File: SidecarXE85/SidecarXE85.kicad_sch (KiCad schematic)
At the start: 11 parts, among them J1 DE9_Plug, J2 DE9_Plug, J3 DE9_Receptacle, J4 Conn_02x08_Odd_Even, J5 DE9_Receptacle, SW1 SW_SPDT, U1 MM74C923, U2 74AHC04

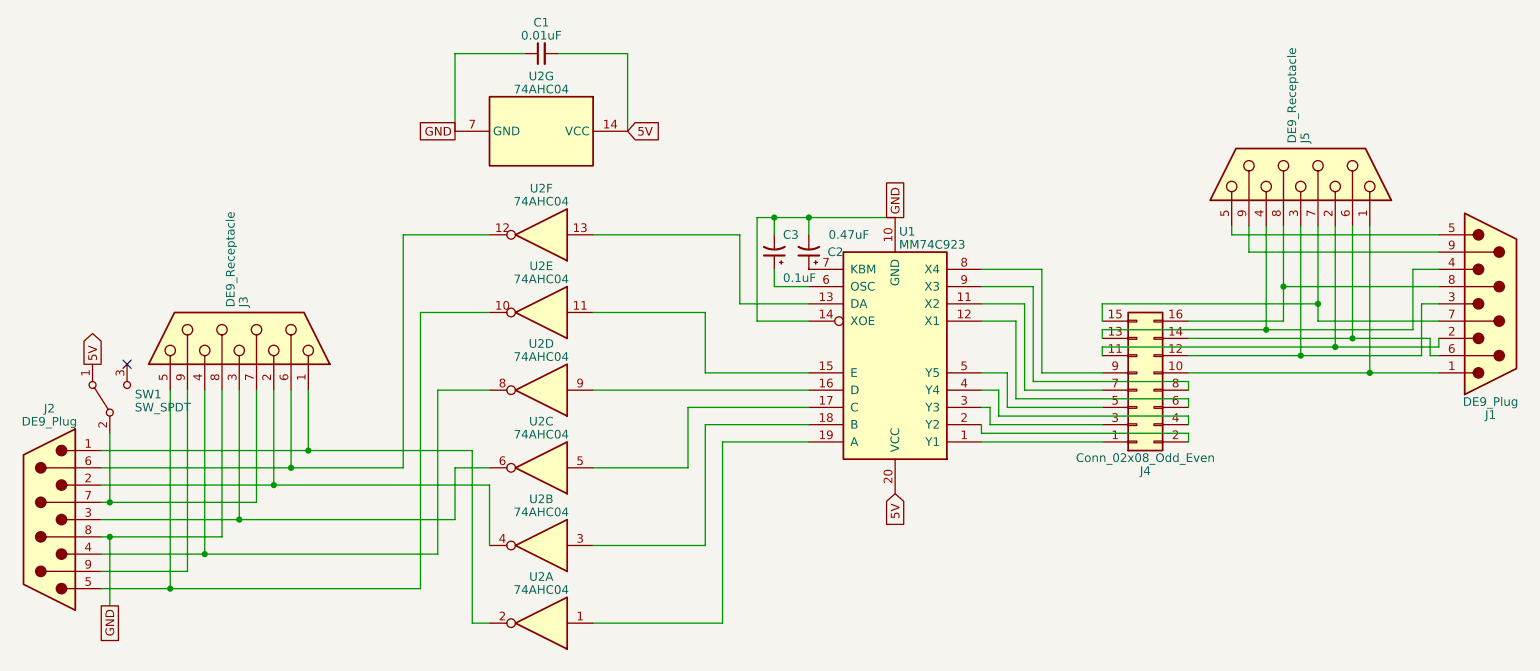
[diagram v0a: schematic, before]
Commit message: Sidecar control board revision 2
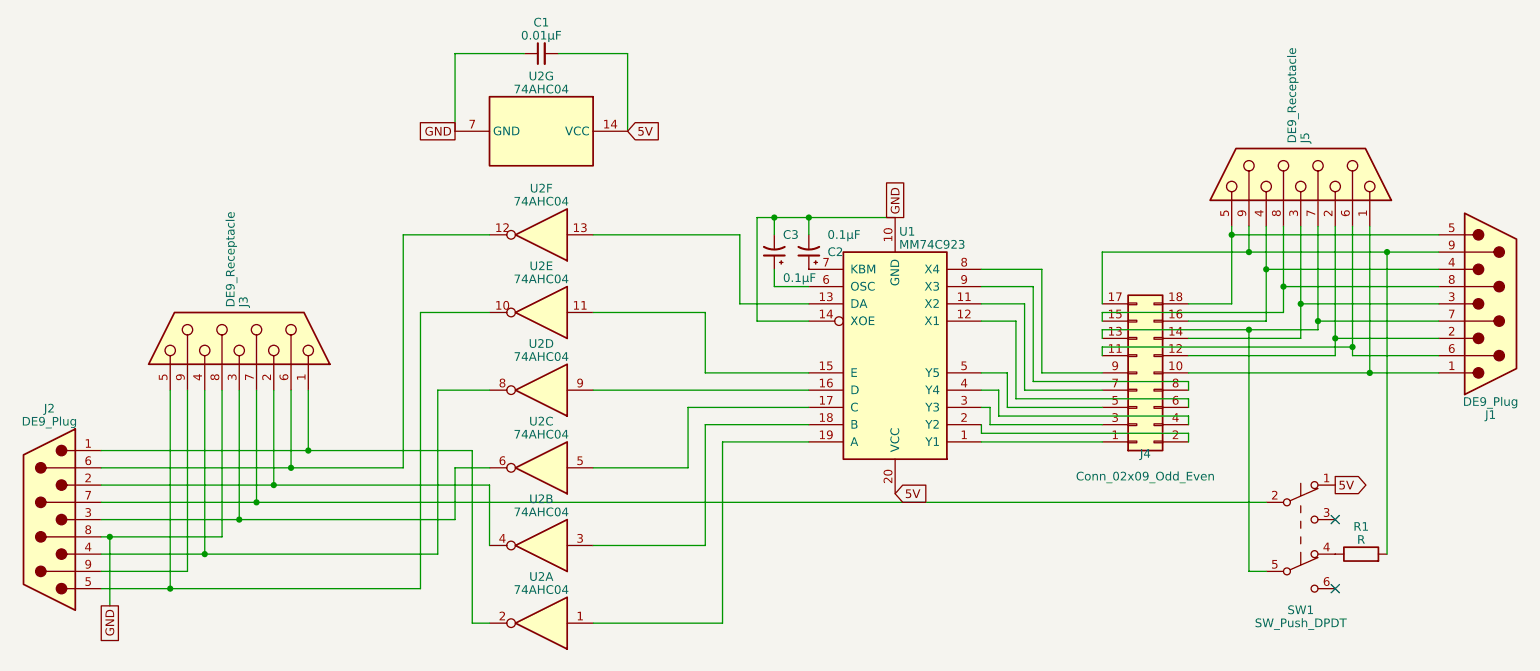
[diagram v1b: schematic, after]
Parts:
- removed SW1: SW_SPDT, Connector_PinHeader_2.54mm:PinHeader_1x03_P2.54mm_Vertical, symbol Switch:SW_SPDT
- added R1: R, Resistor_THT:R_Axial_DIN0207_L6.3mm_D2.5mm_P10.16mm_Horizontal, symbol Device:R
- added SW1: SW_Push_DPDT, Button_Switch_THT:SW_CuK_JS202011AQN_DPDT_Angled, symbol Switch:SW_Push_DPDT
- C1: value 0.01uF -> 0.01µF
- C2: value 0.47uF -> 0.1µF
- C3: value 0.1uF -> 0.1µF
- J4: value Conn_02x08_Odd_Even -> Conn_02x09_Odd_Even; footprint Connector_IDC:IDC-Header_2x08_P2.54mm_Horizontal -> Connector_TE-Connectivity:TE_Micro-MaTch_1-215079-8_2x09_P1.27mm_Vertical; symbol Connector_Generic:Conn_02x08_Odd_Even -> Connector_Generic:Conn_02x09_Odd_Even
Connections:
- net 5V: now also SW1.1 (A)
- net at J2.7, J3.7: now also SW1.2 (B)
- net at J1.2, J5.2: now also J4.12 (Pin_12); no longer J4.11 (Pin_11)
- net at J1.3, J5.3: now also J4.14 (Pin_14); no longer J4.12 (Pin_12)
- net at J1.4, J5.4: now also J4.16 (Pin_16); no longer J4.13 (Pin_13)
- net at J1.5, J5.5: now also J4.18 (Pin_18)
- net at J1.6, J5.6: now also J4.11 (Pin_11); no longer J4.14 (Pin_14)
- net at J1.7, J5.7: now also J4.13 (Pin_13), SW1.5 (B); no longer J4.15 (Pin_15)
- net at J1.8, J5.8: now also J4.15 (Pin_15); no longer J4.16 (Pin_16)
- net at J1.9, J5.9: now also J4.17 (Pin_17), R1.2
- new net: R1.1, SW1.4 (A)
- no-connect marks 1 -> 2
